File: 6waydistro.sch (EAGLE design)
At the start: 36 parts, among them J1 POWERPOLE_POWER10AWG, J10 FUSEATC, J11 POWERPOLE_POWER10AWG, J12 FUSEATC, J2 FUSEATC, J3 POWERPOLE_POWER10AWG, J4 FUSEATC, J5 POWERPOLE_POWER10AWG, J6 FUSEATC, J7 POWERPOLE_POWER10AWG, J8 FUSEATC, J9 POWERPOLE_POWER10AWG

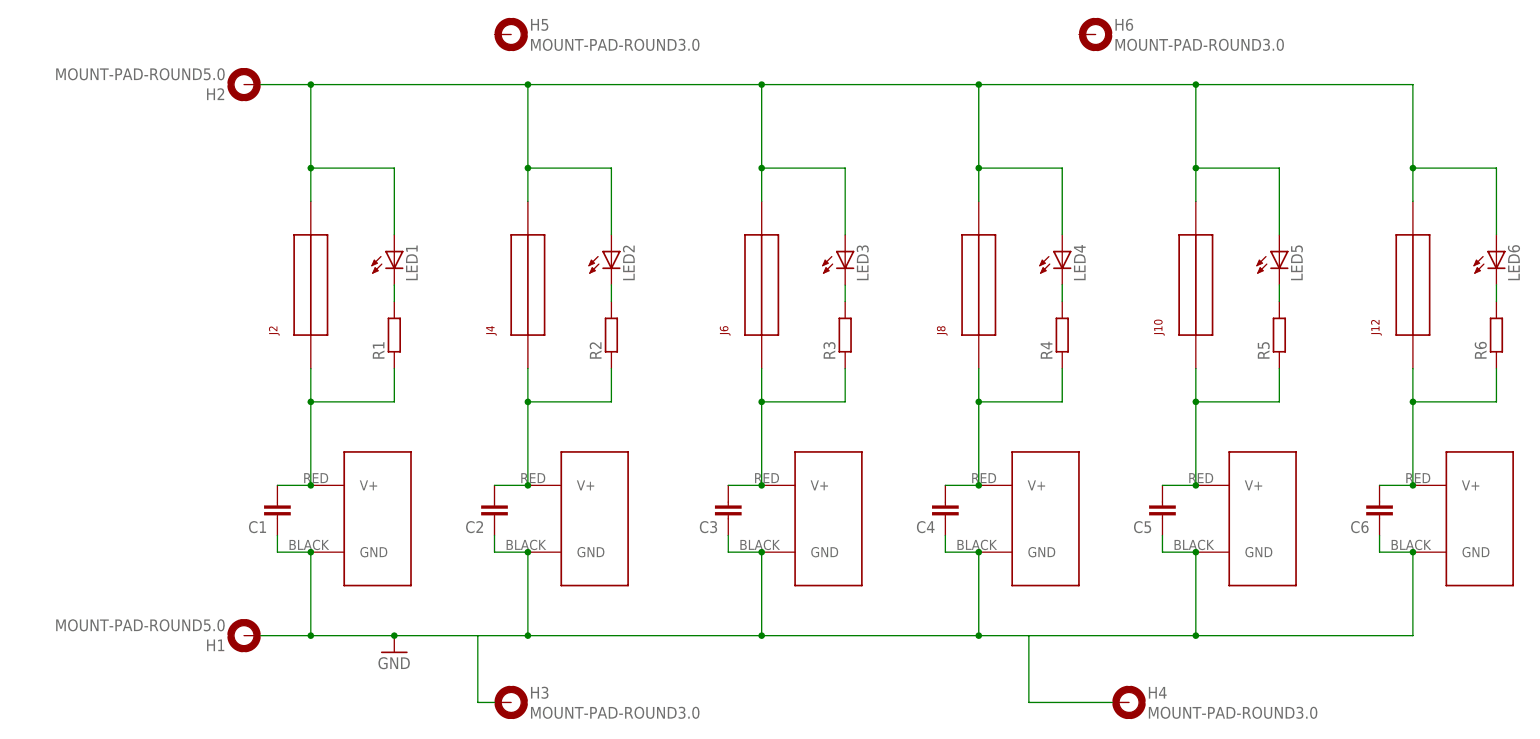
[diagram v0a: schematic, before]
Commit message: Removed wire inlet holes and adjusted board layout for acrylic case
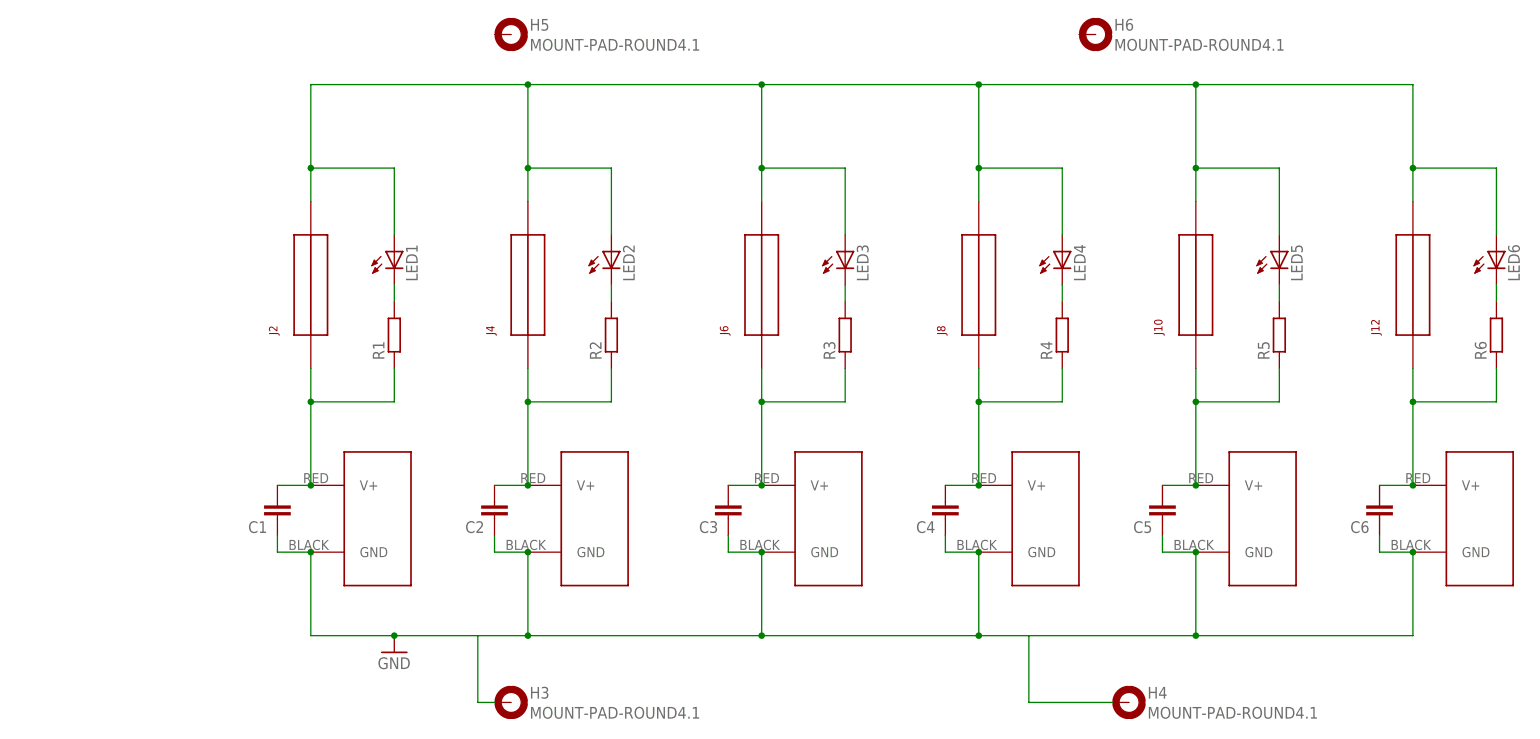
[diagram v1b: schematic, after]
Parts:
- removed H1, H2: MOUNT-PAD-ROUND5.0, holes:MOUNT-PAD-ROUND5.0
- H3, H4, H5, H6: value MOUNT-PAD-ROUND3.0 -> MOUNT-PAD-ROUND4.1; device holes:MOUNT-PAD-ROUND3.0 -> holes:MOUNT-PAD-ROUND4.1
- J1, J11, J3, J5, J7, J9: value POWERPOLE_POWER10AWG -> POWERPOLE_POWER45A; device powerpoles:POWERPOLE_POWER10AWG -> powerpoles:POWERPOLE_POWER45A
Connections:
- net GND: no longer H1.MOUNT
- net VCC: no longer H2.MOUNT
